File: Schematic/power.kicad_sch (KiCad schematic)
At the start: 11 parts, among them J3 Conn_01x03_Pin, U2 LM2678S-12, U5 LD1117S33TR_SOT223

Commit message: Most of the schematic and PCB layout.
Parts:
- added LD1: LED_Green, LED_THT:LED_D5.0mm, symbol stm32f091-rescue:LED_Small_ALT-Device
- added LD1: LED_Red, LED_THT:LED_D5.0mm, symbol stm32f091-rescue:LED_Small_ALT-Device
- added LD1: LED_Blue, LED_THT:LED_D5.0mm, symbol stm32f091-rescue:LED_Small_ALT-Device
- added R1 (x2): 5.6k, Resistor_SMD:R_1206_3216Metric_Pad1.30x1.75mm_HandSolder, symbol Device:R_US
- added R1: 56k, Resistor_SMD:R_1206_3216Metric_Pad1.30x1.75mm_HandSolder, symbol Device:R_US
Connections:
- net +12V: now also R1.1
- net +5V: now also R1.1
- net GND: now also LD1.1 (K), LD1.1 (K), LD1.1 (K)
- net VA: now also R1.1
- net VSW: now reaches Cb1.2, D1.1 (K), L1.1, U2.1 (VSW)
- new net: LD1.2 (A), R1.2 (x3)

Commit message: Added stuff from today
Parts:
- J3: footprint Connector_PinHeader_2.54mm:PinHeader_1x03_P2.54mm_Vertical -> Connector_PinSocket_2.54mm:PinSocket_1x03_P2.54mm_Vertical
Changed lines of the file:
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@@
+    )
+  )
+  (symbol (lib_id "power:GND") (at 110.49 107.95 0) (unit 1)
+    (in_bom yes) (on_board yes) (dnp no)
+    (property "Reference" "#PWR0130" (at 110.49 114.3 0)
+      (effects (font (size 1.27 1.27)) hide)
+    )
+    (property "Value" "GND" (at 110.617 112.3442 0)
+      (effects (font (size 1.27 1.27)))
+    )
+    (property "Footprint" "" (at 110.49 107.95 0)
+      (effects (font (size 1.27 1.27)) hide)
+    )
+    (property "Datasheet" "" (at 110.49 107.95 0)
+      (effects (font (size 1.27 1.27)) hide)
+    )
+    (pin "1")
+    (instances
+      (project "stm32f091"
+        (path "/1a854c3f-f20e-4271-9c06-678b7140bb2e"
+          (reference "#PWR0130") (unit 1)
+        )
+      )
+      (project "Schematic"
+        (path "/ced54cd9-3b34-40e4-aa66-964aaab81b0a/49528601-a054-44d2-8cd6-b055d7d9a1ef"
+          (reference "#PWR011") (unit 1)
+        )
+        (path "/ced54cd9-3b34-40e4-aa66-964aaab81b0a"
+          (reference "#PWR019") (unit 1)
+        )
+        (path "/ced54cd9-3b34-40e4-aa66-964aaab81b0a/1629468b-8e9d-4ab7-97ca-858e6989be67"
+          (reference "#PWR024") (unit 1)
+        )
+        (path "/ced54cd9-3b34-40e4-aa66-964aaab81b0a/575551e4-af3a-490e-80f8-c842b6f0dfe5"
+          (reference "#PWR024") (unit 1)
+        )
+        (path "/ced54cd9-3b34-40e4-aa66-964aaab81b0a/17b7dae5-2f82-4d17-9b49-7ea60414647f"
+          (reference "#PWR023") (unit 1)
+        )
+      )
     )
   )
@@
     )
   )
+  (symbol (lib_id "power:GND") (at 138.43 109.22 0) (unit 1)
+    (in_bom yes) (on_board yes) (dnp no)
+    (property "Reference" "#PWR0130" (at 138.43 115.57 0)
+      (effects (font (size 1.27 1.27)) hide)
+    )
+    (property "Value" "GND" (at 138.557 113.6142 0)
+      (effects (font (size 1.27 1.27)))
+    )
+    (property "Footprint" "" (at 138.43 109.22 0)
+      (effects (font (size 1.27 1.27)) hide)
+    )
+    (property "Datasheet" "" (at 138.43 109.22 0)
+      (effects (font (size 1.27 1.27)) hide)
+    )
+    (pin "1")
+    (instances
+      (project "stm32f091"
+        (path "/1a854c3f-f20e-4271-9c06-678b7140bb2e"
+          (reference "#PWR0130") (unit 1)
+        )
+      )
+      (project "Schematic"
+        (path "/ced54cd9-3b34-40e4-aa66-964aaab81b0a/49528601-a054-44d2-8cd6-b055d7d9a1ef"
+          (reference "#PWR011") (unit 1)
+        )
+        (path "/ced54cd9-3b34-40e4-aa66-964aaab81b0a"
+          (reference "#PWR019") (unit 1)
+        )
+        (path "/ced54cd9-3b34-40e4-aa66-964aaab81b0a/1629468b-8e9d-4ab7-97ca-858e6989be67"
+          (reference "#PWR024") (unit 1)
+        )
+        (path "/ced54cd9-3b34-40e4-aa66-964aaab81b0a/575551e4-af3a-490e-80f8-c842b6f0dfe5"
+          (reference "#PWR024") (unit 1)
+        )
+        (path "/ced54cd9-3b34-40e4-aa66-964aaab81b0a/17b7dae5-2f82-4d17-9b49-7ea60414647f"
+          (reference "#PWR025") (unit 1)
+        )
+      )
+    )
+  )
   (symbol (lib_id "stm32f091-rescue:LED_Small_ALT-Device") (at 220.98 41.91 90) (unit 1)
     (in_bom yes) (on_board yes) (dnp no)
@@
     )
   )
-  (symbol (lib_id "power:GND") (at 138.43 109.22 0) (unit 1)
-    (in_bom yes) (on_board yes) (dnp no)
-    (property "Reference" "#PWR0115" (at 138.43 115.57 0)
-      (effects (font (size 1.27 1.27)) hide)
-    )
-    (property "Value" "GND" (at 138.557 113.6142 0)
-      (effects (font (size 1.27 1.27)) hide)
-    )
-    (property "Footprint" "" (at 138.43 109.22 0)
-      (effects (font (size 1.27 1.27)) hide)
-    )
-    (property "Datasheet" "" (at 138.43 109.22 0)
+  (symbol (lib_id "stm32f091-rescue:LED_Small_ALT-Device") (at 138.43 106.68 90) (unit 1)
+    (in_bom yes) (on_board yes) (dnp no)
+    (property "Reference" "LD1" (at 140.208 105.5116 90)
+      (effects (font (size 1.27 1.27)) (justify right))
+    )
+    (property "Value" "LED_Red" (at 140.208 107.823 90)
+      (effects (font (size 1.27 1.27)) (justify right))
+    )
+    (property "Footprint" "LED_THT:LED_D5.0mm" (at 138.43 106.68 90)
+      (effects (font (size 1.27 1.27)) hide)
+    )
+    (property "Datasheet" "" (at 138.43 106.68 90)
+      (effects (font (size 1.27 1.27)) hide)
+    )
+    (pin "1")
+    (pin "2")
+    (instances
+      (project "stm32f091"
+        (path "/5ce0f945-8ce0-4168-b91a-66b013b0da45"
+          (reference "LD1") (unit 1)
+        )
+      )
+      (project "Schematic"
+        (path "/ced54cd9-3b34-40e4-aa66-964aaab81b0a/49528601-a054-44d2-8cd6-b055d7d9a1ef"
+          (reference "LD1") (unit 1)
+        )
+        (path "/ced54cd9-3b34-40e4-aa66-964aaab81b0a/1629468b-8e9d-4ab7-97ca-858e6989be67"
+          (reference "LD2") (unit 1)
+        )
+        (path "/ced54cd9-3b34-40e4-aa66-964aaab81b0a/17b7dae5-2f82-4d17-9b49-7ea60414647f"
+          (reference "LD5") (unit 1)
+        )
+      )
+    )
+  )
+  (symbol (lib_id "power:GND") (at 52.07 63.5 0) (unit 1)
+    (in_bom yes) (on_board yes) (dnp no)
+    (property "Reference" "#PWR0115" (at 52.07 69.85 0)
+      (effects (font (size 1.27 1.27)) hide)
+    )
+    (property "Value" "GND" (at 52.197 67.8942 0)
+      (effects (font (size 1.27 1.27)) hide)
+    )
+    (property "Footprint" "" (at 52.07 63.5 0)
+      (effects (font (size 1.27 1.27)) hide)
+    )
+    (property "Datasheet" "" (at 52.07 63.5 0)
       (effects (font (size 1.27 1.27)) hide)
     )
@@
         )
         (path "/ced54cd9-3b34-40e4-aa66-964aaab81b0a/17b7dae5-2f82-4d17-9b49-7ea60414647f"
-          (reference "#PWR047") (unit 1)
-        )
-      )
-    )
-  )
-  (symbol (lib_id "stm32f091-rescue:LED_Small_ALT-Device") (at 138.43 106.68 90) (unit 1)
-    (in_bom yes) (on_board yes) (dnp no)
-    (property "Reference" "LD1" (at 140.208 105.5116 90)
-      (effects (font (size 1.27 1.27)) (justify right))
-    )
-    (property "Value" "LED_Red" (at 140.208 107.823 90)
-      (effects (font (size 1.27 1.27)) (justify right))
-    )
-    (property "Footprint" "LED_THT:LED_D5.0mm" (at 138.43 106.68 90)
-      (effects (font (size 1.27 1.27)) hide)
-    )
-    (property "Datasheet" "" (at 138.43 106.68 90)
-      (effects (font (size 1.27 1.27)) hide)
-    )
-    (pin "1")
-    (pin "2")
-    (instances
-      (project "stm32f091"
-        (path "/5ce0f945-8ce0-4168-b91a-66b013b0da45"
-          (reference "LD1") (unit 1)
-        )
-      )
-      (project "Schematic"
-        (path "/ced54cd9-3b34-40e4-aa66-964aaab81b0a/49528601-a054-44d2-8cd6-b055d7d9a1ef"
-          (reference "LD1") (unit 1)
-        )
-        (path "/ced54cd9-3b34-40e4-aa66-964aaab81b0a/1629468b-8e9d-4ab7-97ca-858e6989be67"
-          (reference "LD2") (unit 1)
-        )
-        (path "/ced54cd9-3b34-40e4-aa66-964aaab81b0a/17b7dae5-2f82-4d17-9b49-7ea60414647f"
-          (reference "LD5") (unit 1)
-        )
-      )
-    )
-  )
-  (symbol (lib_id "power:GND") (at 52.07 63.5 0) (unit 1)
-    (in_bom yes) (on_board yes) (dnp no)
-    (property "Reference" "#PWR0115" (at 52.07 69.85 0)
-      (effects (font (size 1.27 1.27)) hide)
-    )
-    (property "Value" "GND" (at 52.197 67.8942 0)
-      (effects (font (size 1.27 1.27)) hide)
-    )
-    (property "Footprint" "" (at 52.07 63.5 0)
-      (effects (font (size 1.27 1.27)) hide)
-    )
-    (property "Datasheet" "" (at 52.07 63.5 0)
-      (effects (font (size 1.27 1.27)) hide)
-    )
-    (pin "1")
-    (instances
-      (project "stm32f091"
-        (path "/5ce0f945-8ce0-4168-b91a-66b013b0da45"
-          (reference "#PWR0115") (unit 1)
-        )
-      )
-      (project "Schematic"
-        (path "/ced54cd9-3b34-40e4-aa66-964aaab81b0a/49528601-a054-44d2-8cd6-b055d7d9a1ef"
-          (reference "#PWR034") (unit 1)
-        )
-        (path "/ced54cd9-3b34-40e4-aa66-964aaab81b0a/1629468b-8e9d-4ab7-97ca-858e6989be67"
-          (reference "#PWR040") (unit 1)
-        )
-        (path "/ced54cd9-3b34-40e4-aa66-964aaab81b0a/17b7dae5-2f82-4d17-9b49-7ea60414647f"
           (reference "#PWR045") (unit 1)
         )
@@
       (effects (font (size 1.27 1.27)))
     )
-    (property "Footprint" "Connector_PinHeader_2.54mm:PinHeader_1x03_P2.54mm_Vertical" (at 35.56 46.99 0)
+    (property "Footprint" "Connector_PinSocket_2.54mm:PinSocket_1x03_P2.54mm_Vertical" (at 35.56 46.99 0)
       (effects (font (size 1.27 1.27)) hide)
     )
@@
         )
       )
-    )
-  )
-  (symbol (lib_id "power:GND") (at 110.49 107.95 0) (unit 1)
-    (in_bom yes) (on_board yes) (dnp no)
-    (property "Reference" "#PWR0101" (at 110.49 114.3 0)
-      (effects (font (size 1.27 1.27)) hide)
-    )
-    (property "Value" "GND" (at 110.617 112.3442 0)
-      (effects (font (size 1.27 1.27)) hide)
-    )
-    (property "Footprint" "" (at 110.49 107.95 0)
-      (effects (font (size 1.27 1.27)) hide)
-    )
-    (property "Datasheet" "" (at 110.49 107.95 0)
-      (effects (font (size 1.27 1.27)) hide)
-    )
-    (pin "1")
-    (instances
-      (project "stm32f091"
-        (path "/1a854c3f-f20e-4271-9c06-678b7140bb2e"
-          (reference "#PWR0101") (unit 1)
-        )
-      )
-      (project "Schematic"
-        (path "/ced54cd9-3b34-40e4-aa66-964aaab81b0a/49528601-a054-44d2-8cd6-b055d7d9a1ef"
-          (reference "#PWR015") (unit 1)
-        )
-        (path "/ced54cd9-3b34-40e4-aa66-964aaab81b0a/17b7dae5-2f82-4d17-9b49-7ea60414647f"
-          (reference "#PWR041") (unit 1)
-        )
-      )

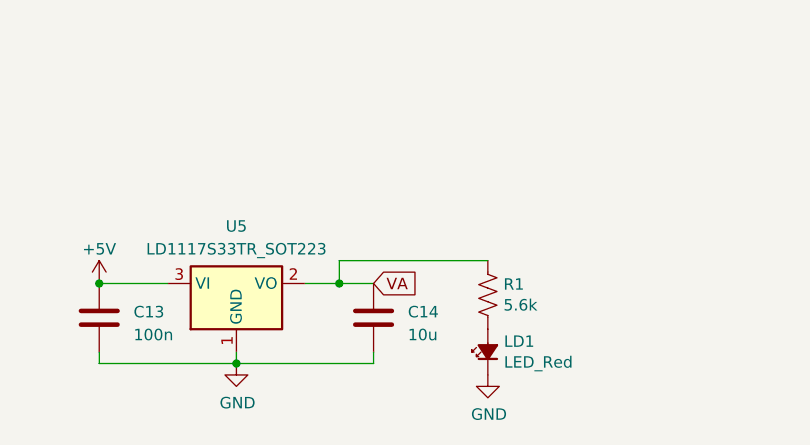
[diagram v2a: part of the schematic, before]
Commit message: Added sensors. Fixed other stuff.
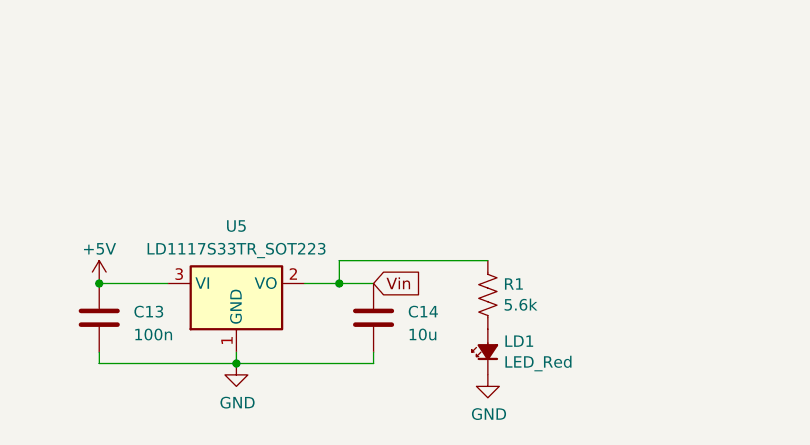
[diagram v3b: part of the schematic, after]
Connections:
- net VA renamed Vin
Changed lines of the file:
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@@
     (effects (font (size 1.27 1.27)) (justify left bottom))
   )
-  (global_label "VA" (shape input) (at 125.73 99.06 0) (fields_autoplaced)
+  (global_label "Vin" (shape input) (at 125.73 99.06 0) (fields_autoplaced)
     (effects (font (size 1.27 1.27)) (justify left))
-    (property "Intersheetrefs" "${INTERSHEET_REFS}" (at 130.813 99.06 0)
+    (property "Intersheetrefs" "${INTERSHEET_REFS}" (at 131.4782 99.06 0)
       (effects (font (size 1.27 1.27)) (justify left) hide)
     )

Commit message: Mostly finallized PCB
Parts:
- added TP1: GND, TestPoint:TestPoint_THTPad_D2.0mm_Drill1.0mm, symbol Connector:TestPoint
- added TP2: 5V, TestPoint:TestPoint_THTPad_D2.0mm_Drill1.0mm, symbol Connector:TestPoint
- added TP3: 12V, TestPoint:TestPoint_THTPad_D2.0mm_Drill1.0mm, symbol Connector:TestPoint
- added TP4: 3V, TestPoint:TestPoint_THTPad_D2.0mm_Drill1.0mm, symbol Connector:TestPoint
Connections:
- net +12V: now also TP3.1
- net +5V: now also TP2.1
- net GND: now also TP1.1
- net Vin: now also TP4.1
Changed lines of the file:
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@@
 (kicad_sch (version 20230121) (generator eeschema)
   (paper "A4")
-  (junction (at 163.83 58.42) (diameter 0) (color 0 0 0 0)
-  )
   (junction (at 80.01 44.45) (diameter 0) (color 0 0 0 0)
   )
@@
   (junction (at 80.01 58.42) (diameter 0) (color 0 0 0 0)
   )
+  (junction (at 158.75 58.42) (diameter 0) (color 0 0 0 0)
+  )
   (junction (at 176.53 26.67) (diameter 0) (color 0 0 0 0)
   )
+  (junction (at 220.98 31.75) (diameter 0) (color 0 0 0 0)
+  )
   (junction (at 176.53 58.42) (diameter 0) (color 0 0 0 0)
   )
+  (junction (at 138.43 96.52) (diameter 0) (color 0 0 0 0)
+  )
   (junction (at 205.74 26.67) (diameter 0) (color 0 0 0 0)
   )
@@
     (stroke (width 0) (type default))
   )
-  (wire (pts (xy 96.52 58.42) (xy 163.83 58.42))
+  (wire (pts (xy 96.52 58.42) (xy 158.75 58.42))
     (stroke (width 0) (type default))
   )
@@
     (stroke (width 0) (type default))
   )
-  (wire (pts (xy 163.83 58.42) (xy 170.18 58.42))
+  (wire (pts (xy 158.75 58.42) (xy 170.18 58.42))
     (stroke (width 0) (type default))
   )
@@
     )
   )
+  (symbol (lib_id "Connector:TestPoint") (at 138.43 96.52 0) (unit 1)
+    (in_bom yes) (on_board yes) (dnp no) (fields_autoplaced)
+    (property "Reference" "TP4" (at 139.827 92.0059 0)
+      (effects (font (size 1.27 1.27)) (justify left))
+    )
+    (property "Value" "3V" (at 139.827 94.4301 0)
+      (effects (font (size 1.27 1.27)) (justify left))
+    )
+    (property "Footprint" "TestPoint:TestPoint_THTPad_D2.0mm_Drill1.0mm" (at 143.51 96.52 0)
+      (effects (font (size 1.27 1.27)) hide)
+    )
+    (property "Datasheet" "~" (at 143.51 96.52 0)
+      (effects (font (size 1.27 1.27)) hide)
+    )
+    (pin "1")
+    (instances
+      (project "Schematic"
+        (path "/ced54cd9-3b34-40e4-aa66-964aaab81b0a/17b7dae5-2f82-4d17-9b49-7ea60414647f"
+          (reference "TP4") (unit 1)
+        )
+      )
+    )
+  )
   (symbol (lib_id "Device:L") (at 194.31 26.67 90) (unit 1)
     (in_bom yes) (on_board yes) (dnp no) (fields_autoplaced)
@@
     )
   )
-  (symbol (lib_id "power:GND") (at 163.83 58.42 0) (unit 1)
-    (in_bom yes) (on_board yes) (dnp no) (fields_autoplaced)
-    (property "Reference" "#PWR01" (at 163.83 64.77 0)
-      (effects (font (size 1.27 1.27)) hide)
-    )
-    (property "Value" "GND" (at 163.83 63.5 0)
+  (symbol (lib_id "power:GND") (at 158.75 58.42 0) (unit 1)
+    (in_bom yes) (on_board yes) (dnp no) (fields_autoplaced)
+    (property "Reference" "#PWR01" (at 158.75 64.77 0)
+      (effects (font (size 1.27 1.27)) hide)
+    )
+    (property "Value" "GND" (at 158.75 63.5 0)
       (effects (font (size 1.27 1.27)))
     )
-    (property "Footprint" "" (at 163.83 58.42 0)
-      (effects (font (size 1.27 1.27)) hide)
-    )
-    (property "Datasheet" "" (at 163.83 58.42 0)
+    (property "Footprint" "" (at 158.75 58.42 0)
+      (effects (font (size 1.27 1.27)) hide)
+    )
+    (property "Datasheet" "" (at 158.75 58.42 0)
       (effects (font (size 1.27 1.27)) hide)
     )
@@
         )
       )
+    )
+  )
+  (symbol (lib_id "Connector:TestPoint") (at 220.98 31.75 0) (unit 1)
+    (in_bom yes) (on_board yes) (dnp no) (fields_autoplaced)
+    (property "Reference" "TP2" (at 222.377 27.2359 0)
+      (effects (font (size 1.27 1.27)) (justify left))
+    )
+    (property "Value" "5V" (at 222.377 29.6601 0)
+      (effects (font (size 1.27 1.27)) (justify left))
+    )
+    (property "Footprint" "TestPoint:TestPoint_THTPad_D2.0mm_Drill1.0mm" (at 226.06 31.75 0)
+      (effects (font (size 1.27 1.27)) hide)
+    )
+    (property "Datasheet" "~" (at 226.06 31.75 0)
+      (effects (font (size 1.27 1.27)) hide)
+    )
+    (pin "1")
+    (instances
+      (project "Schematic"
+        (path "/ced54cd9-3b34-40e4-aa66-964aaab81b0a/17b7dae5-2f82-4d17-9b49-7ea60414647f"
+          (reference "TP2") (unit 1)
+        )
+      )
+    )
+  )
+  (symbol (lib_id "Connector:TestPoint") (at 52.07 44.45 0) (unit 1)
+    (in_bom yes) (on_board yes) (dnp no) (fields_autoplaced)
+    (property "Reference" "TP3" (at 53.467 39.9359 0)
+      (effects (font (size 1.27 1.27)) (justify left))
+    )
+    (property "Value" "12V" (at 53.467 42.3601 0)
+      (effects (font (size 1.27 1.27)) (justify left))
+    )
+    (property "Footprint" "TestPoint:TestPoint_THTPad_D2.0mm_Drill1.0mm" (at 57.15 44.45 0)
+      (effects (font (size 1.27 1.27)) hide)
+    )
+    (property "Datasheet" "~" (at 57.15 44.45 0)
+      (effects (font (size 1.27 1.27)) hide)
+    )
+    (pin "1")
+    (instances
+      (project "Schematic"
+        (path "/ced54cd9-3b34-40e4-aa66-964aaab81b0a/17b7dae5-2f82-4d17-9b49-7ea60414647f"
+          (reference "TP3") (unit 1)
+        )
+      )
+    )
+  )
+  (symbol (lib_id "Connector:TestPoint") (at 158.75 58.42 0) (unit 1)
+    (in_bom yes) (on_board yes) (dnp no) (fields_autoplaced)
+    (property "Reference" "TP1" (at 160.147 53.9059 0)
+      (effects (font (size 1.27 1.27)) (justify left))
+    )
+    (property "Value" "GND" (at 160.147 56.3301 0)
+      (effects (font (size 1.27 1.27)) (justify left))
+    )
+    (property "Footprint" "TestPoint:TestPoint_THTPad_D2.0mm_Drill1.0mm" (at 163.83 58.42 0)
+      (effects (font (size 1.27 1.27)) hide)
+    )
+    (property "Datasheet" "~" (at 163.83 58.42 0)
+      (effects (font (size 1.27 1.27)) hide)
+    )
+    (pin "1")
+    (instances
+      (project "Schematic"
+        (path "/ced54cd9-3b34-40e4-aa66-964aaab81b0a/17b7dae5-2f82-4d17-9b49-7ea60414647f"
+          (reference "TP1") (unit 1)
+        )
+      )
